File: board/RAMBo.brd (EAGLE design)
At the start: 104.1 x 102.9 mm, 264 parts, among them Q1 PSMN7R0-60YS, Q2 PSMN7R0-60YS, Q3 PSMN7R0-60YS, Q4 IRLML6346TRPBF, Q5 PSMN7R0-60YS, Q8 IRLML6346TRPBF, U1 ATMEGA32U2-MUR, U2 ATMEGA2560-16AU, U3 TPS54332DDA, U4 AD5206, U5 A4982, U6 A4982, U7 A4982, U8 A4982, U9 A4982, X1 C-GRID-02-70543, X10 C-GRID-04-70543, X11 MSTBV10, X12 SPI, X13 EXT-2, X14 C-GRID-04-70543, X15 C-GRID-04-70543, X16 32u2 EXT, X17 3x2M, X18 3x2M, X19 Analog-Ext, X2 USB B-TH, X20 M05PTH, X21 C-GRID-03-70543, X22 C-GRID-03-70543, X23 C-GRID-03-70543, X24 C-GRID-03-70543, X25 C-GRID-03-70543, X26 C-GRID-03-70543, X27 C-GRID-02-70543, X28 C-GRID-02-70543, X29 C-GRID-02-70543, X3 C-GRID-02-70543, X30 C-GRID-02-70543, X31 M05PTH, X32 M05PTH, X33 MSTBA6, X34 PWM_EXT, X39 M05X2PTH, X4 C-GRID-04-70543, X5 C-GRID-02-70543, X6 C-GRID-04-70543, X7 C-GRID-04-70543, X8 C-GRID-04-70543, X9 C-GRID-02-70543, Y1 16MHz KX-7, Y2 16MHz KX-7

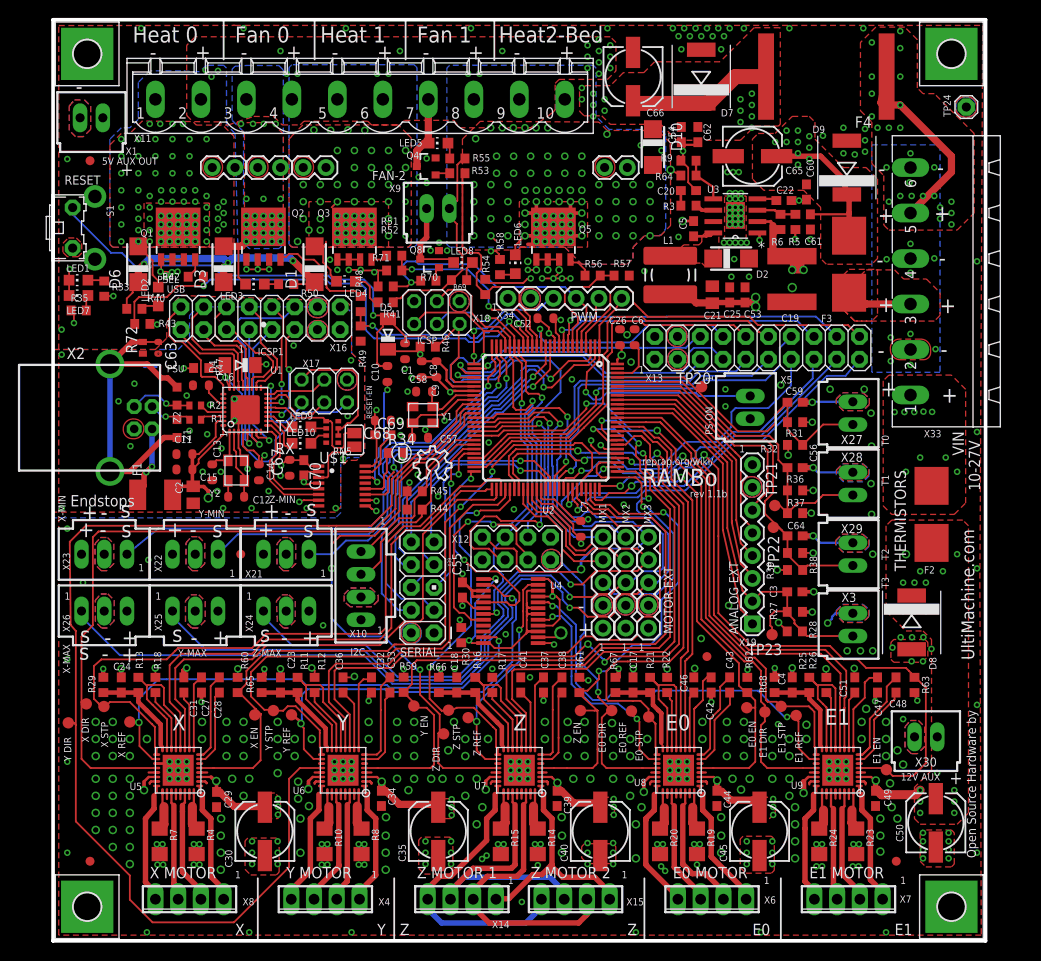
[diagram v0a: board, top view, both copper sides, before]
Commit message: rotate motor and serial ext for easier wave solder
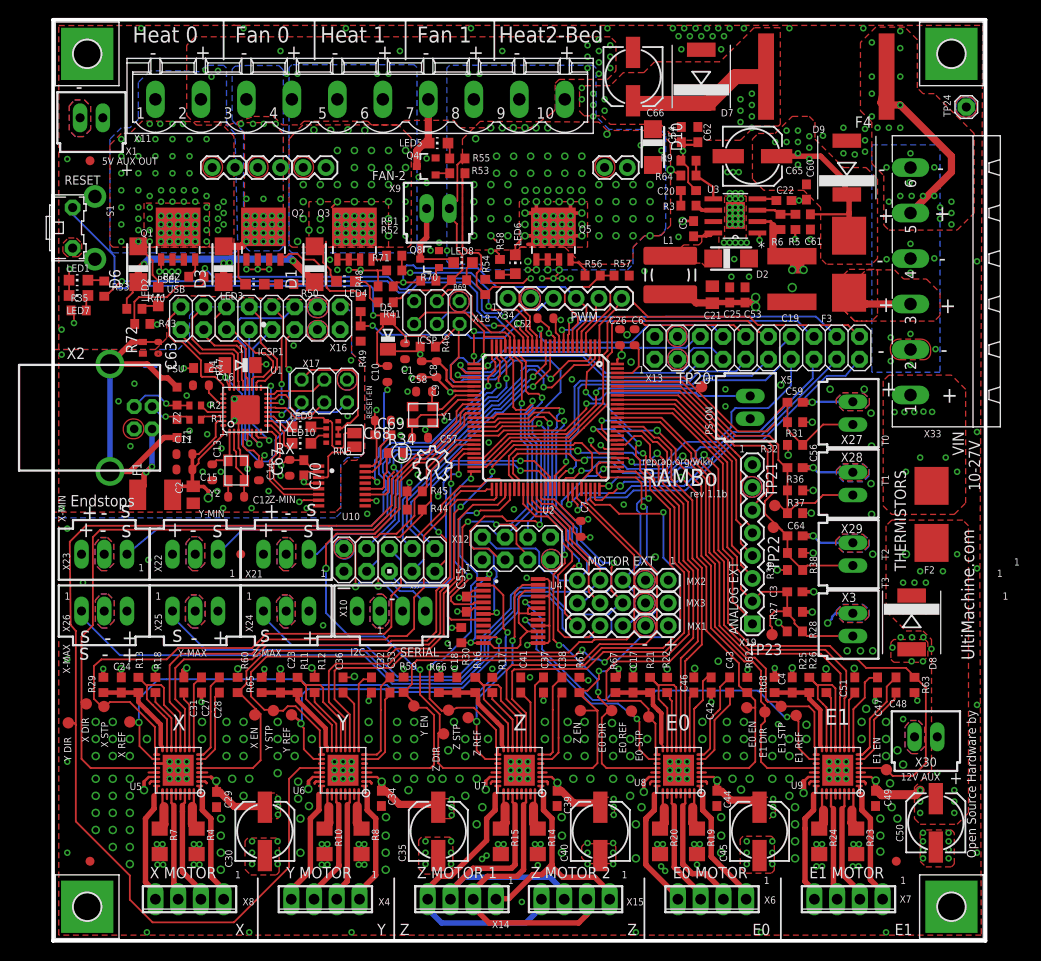
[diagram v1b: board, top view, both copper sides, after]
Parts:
- removed FID5: FIDUCIAL1X2, SparkFun:FIDUCIAL-1X2
- moved X20 7.29 mm to (68.7, 35.2), turned to 180 degrees
- moved X32 5.79 mm to (68.7, 40.3), turned to 180 degrees
- moved X31 5.52 mm to (68.7, 37.7), turned to 180 degrees
- moved X39 4.82 mm to (37.6, 42.5), turned to 90 degrees
- moved X10 4.41 mm to (37.8, 36.8), turned to 0 degrees
- moved C55 1.65 mm to (46.2, 37.6)
- moved R42 0.06 mm to (16.0, 74.2)
- renumbered U$1 to U10
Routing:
- net L13: track 15.4 -> 64.6 mm
- net PC7: track 78.9 -> 61.7 mm, vias 1 -> 0
- net SCL: track 20.1 -> 35.3 mm, vias 0 -> 1
- net PL3: track 57.4 -> 45.3 mm, vias 2 -> 1
- net PC5: track 14.5 -> 25.0 mm
- net PA1: track 94.5 -> 84.3 mm
- net PL5: track 26.4 -> 34.9 mm, vias 1 -> 2
- net TX0: track 55.4 -> 47.0 mm
- net Y-MS2: track 71.1 -> 63.9 mm
- net RX0: track 52.3 -> 45.3 mm
- net PL4: track 30.4 -> 37.2 mm
- net RX1: track 18.1 -> 24.4 mm
- net PB2_MOSI: track 51.8 -> 58.0 mm
- net TX1: track 20.3 -> 25.8 mm
- net Y-EN: track 74.4 -> 69.7 mm
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
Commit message: final connector move, change mount hole for wave
fix drc and silk errors, misc fixes
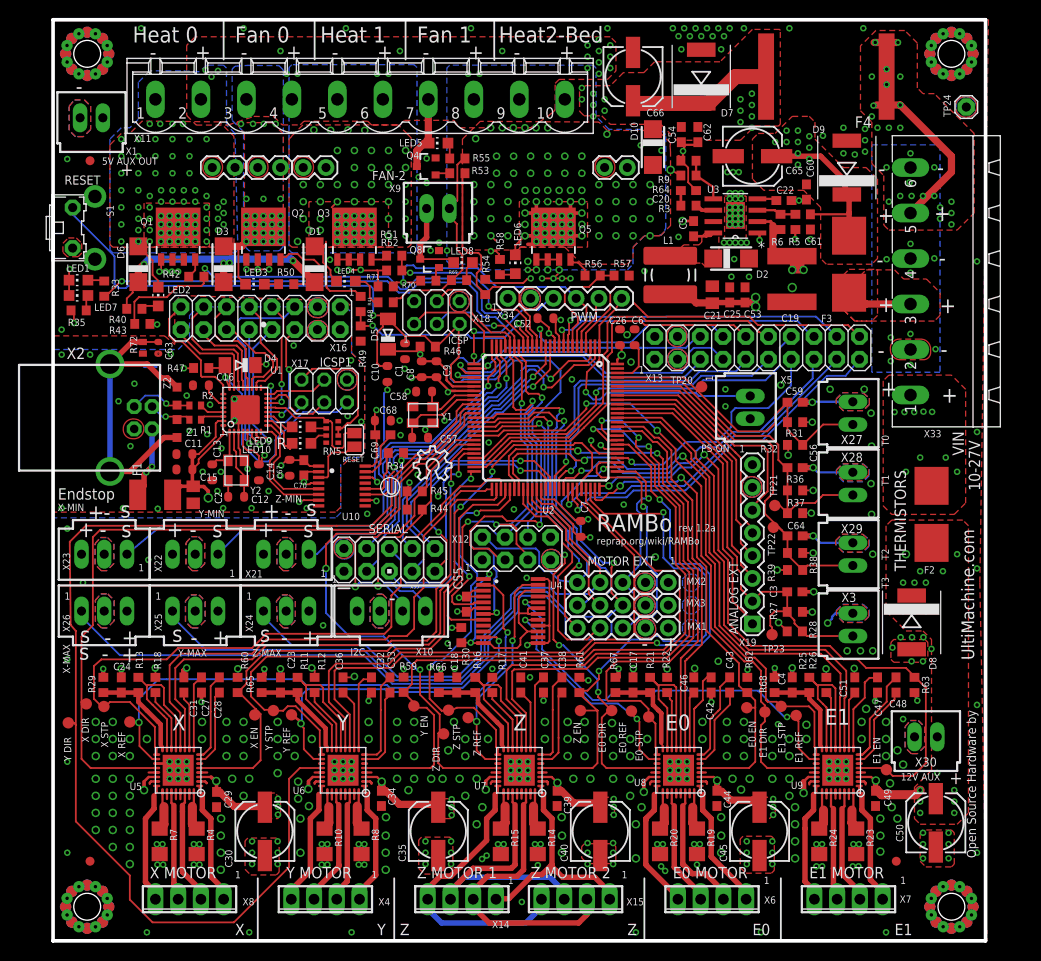
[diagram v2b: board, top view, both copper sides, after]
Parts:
- removed FID4: FIDUCIAL1X2, SparkFun:FIDUCIAL-1X2
- removed H5: MOUNT-PAD-SQUARE3.0, holes:3,0-PAD-SQUARE
- added H4: WAVE-HOLE, ultimachine:3,0-WAVE-HOLE
- H1, H2, H3: value MOUNT-PAD-SQUARE3.0 -> WAVE-HOLE; device holes:3,0-PAD-SQUARE -> ultimachine:3,0-WAVE-HOLE
- moved X32 0.25 mm to (68.7, 40.0)
- moved X20 0.25 mm to (68.7, 34.9)
- moved X31 0.25 mm to (68.7, 37.5)
- renumbered FID6 to FID3
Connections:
- net GND: now also H1.P$1, H1.P$10, H1.P$11, H1.P$12, H1.P$13, H1.P$14, H1.P$15, H1.P$16, H1.P$17, H1.P$18, H1.P$19, H1.P$2, H1.P$20, H1.P$21, H1.P$22, H1.P$23, H1.P$24, H1.P$3, H1.P$4, H1.P$5, H1.P$6, H1.P$7, H1.P$8, H1.P$9, H2.P$1, H2.P$10, H2.P$11, H2.P$12, H2.P$13, H2.P$14, H2.P$15, H2.P$16, H2.P$17, H2.P$18, H2.P$19, H2.P$2, H2.P$20, H2.P$21, H2.P$22, H2.P$23, H2.P$24, H2.P$3, H2.P$4, H2.P$5, H2.P$6, H2.P$7, H2.P$8, H2.P$9, H3.P$1, H3.P$10, H3.P$11, H3.P$12, H3.P$13, H3.P$14, H3.P$15, H3.P$16, H3.P$17, H3.P$18, H3.P$19, H3.P$2, H3.P$20, H3.P$21, H3.P$22, H3.P$23, H3.P$24, H3.P$3, H3.P$4, H3.P$5, H3.P$6, H3.P$7, H3.P$8, H3.P$9, H4.P$1, H4.P$10, H4.P$11, H4.P$12, H4.P$13, H4.P$14, H4.P$15, H4.P$16, H4.P$17, H4.P$18, H4.P$19, H4.P$2, H4.P$20, H4.P$21, H4.P$22, H4.P$23, H4.P$24, H4.P$3, H4.P$4, H4.P$5, H4.P$6, H4.P$7, H4.P$8, H4.P$9; no longer H1.B3,0, H2.B3,0, H3.B3,0, H5.B3,0
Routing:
- net Z-EN: track 56.0 -> 62.4 mm
- net Y-EN: track 69.7 -> 74.6 mm
- net N$16: track 21.6 -> 24.7 mm, vias 21 -> 22
- net Y-MS1: track 79.2 -> 81.1 mm
- net Z-MS1: track 62.1 -> 63.9 mm
- net Z-MS2: track 62.0 -> 63.3 mm
- net GND: track 140.6 -> 141.5 mm, vias 458 -> 456
- net E0-STEP: track 68.9 -> 68.3 mm
- net GND1: vias 25 -> 30
- added copper zone on layer 15, net GND
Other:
- board text added: "Endstop"
- board text added: "R"
- board text added: "T"
- board text added: "reprap.org/wiki/RAMBo"
- board text added: "rev 1.2a"
- board text removed: "Endstops"
- board text removed: "PSEL"
- board text removed: "PSU"
- board text removed: "RESET-EN"
- board text removed: "RX"
- board text removed: "TX"
- board text removed: "USB"
- board text removed: "reprap.org/wiki/"
- board text removed: "rev 1.1b"

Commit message: fix gnd fence
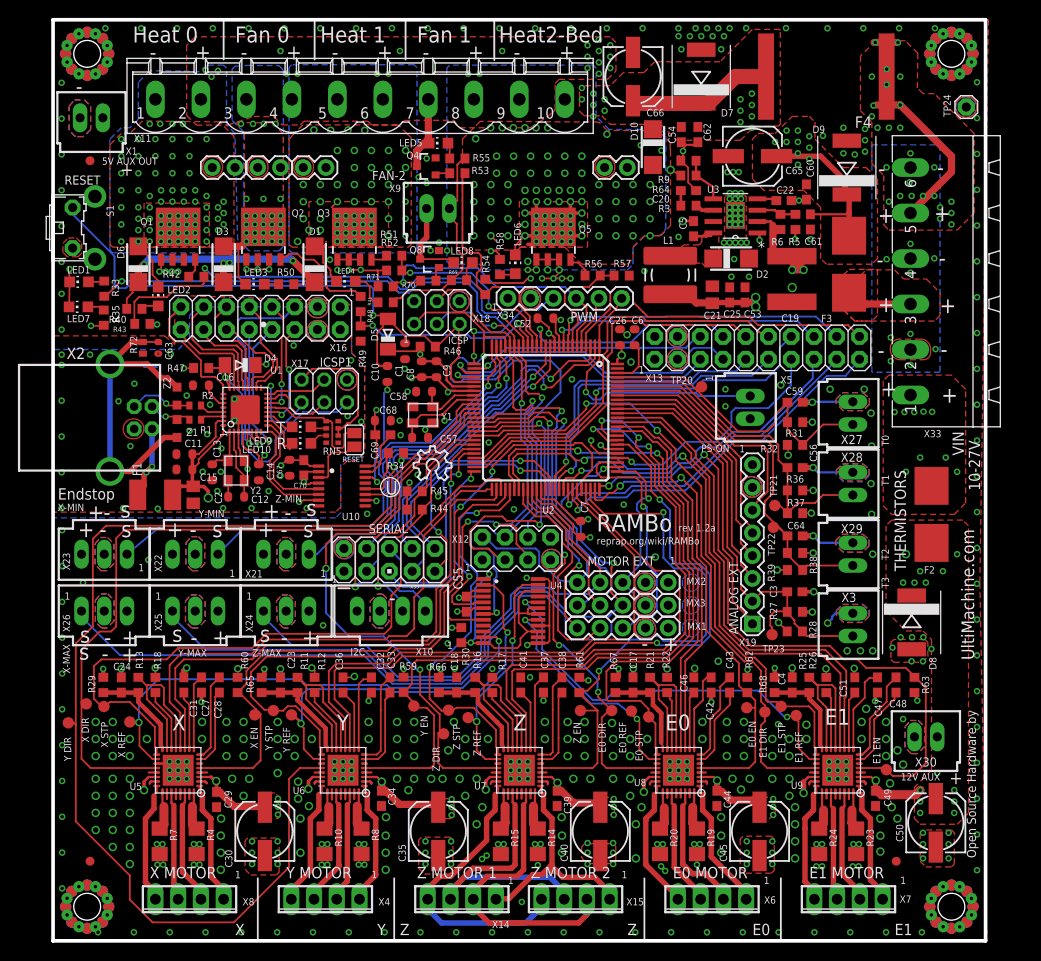
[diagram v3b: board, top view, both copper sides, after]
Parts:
- moved R35 2.92 mm to (5.67, 69.6), turned to 90 degrees
- moved LED7 1.27 mm to (2.84, 70.8)
- moved LED1 0.20 mm to (2.90, 73.6)
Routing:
- net Y-DIR: track 132.9 -> 131.1 mm
- net GND: track 141.5 -> 142.8 mm, vias 456 -> 518
- net X-DIR: track 85.7 -> 84.9 mm
- net GND1: vias 30 -> 34
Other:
- board text added: "Other Layers GTP ---Top Solder Paste OLN -- Board outline TXT -- Drill 2.4 leading suppression"
- board text added: "Panelize with second PCB here."
- board text added: "Stack Up GTO ------ Top Silk GTS - Solder Mask GTL------------ 1oz 0.61mm G2L ----------- 2oz 0.2mm G3L ----------- 2oz 0.61mm GBL ----------- 1oz GBS - Solder Mask Total Thickness ~ 1.62mm"

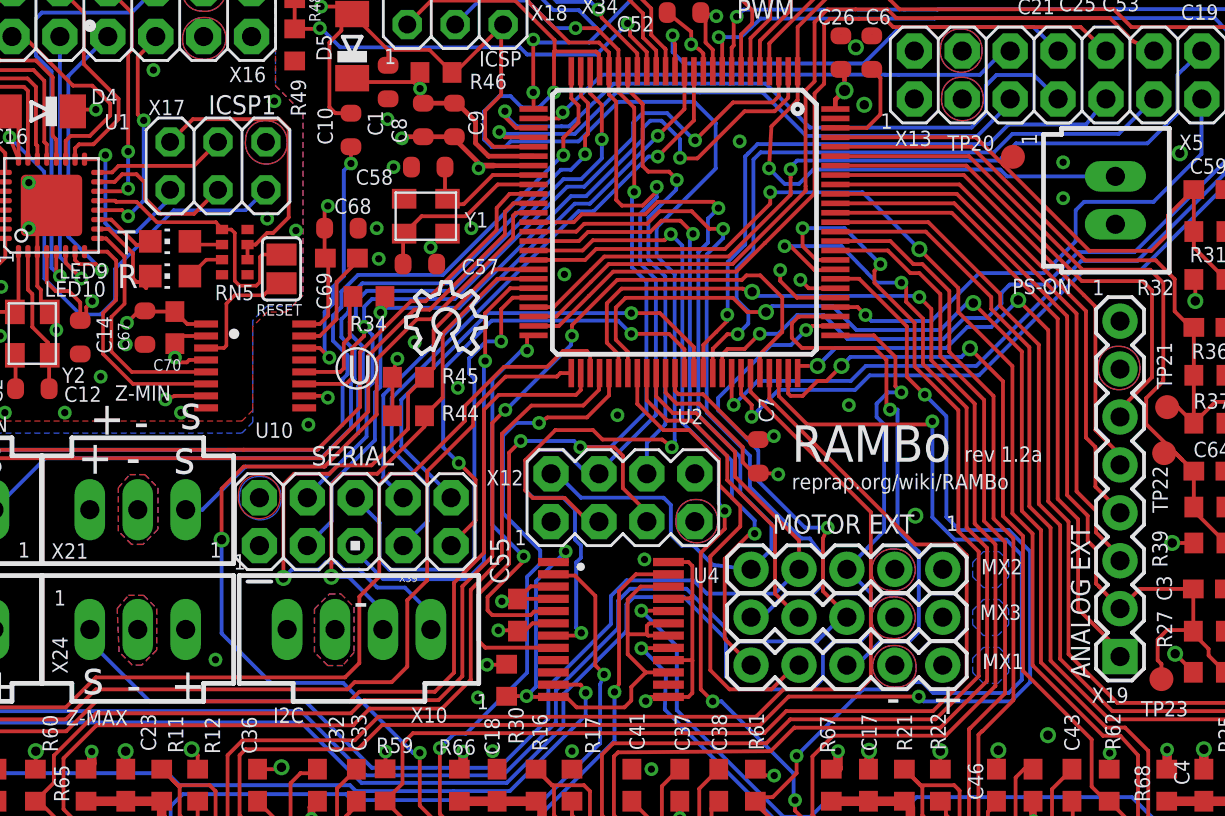
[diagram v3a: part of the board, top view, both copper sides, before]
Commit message: change thieve style, rst-en trace added back,
DTR resistor now pull up - now back to original usb reset behaviour of
Rambo
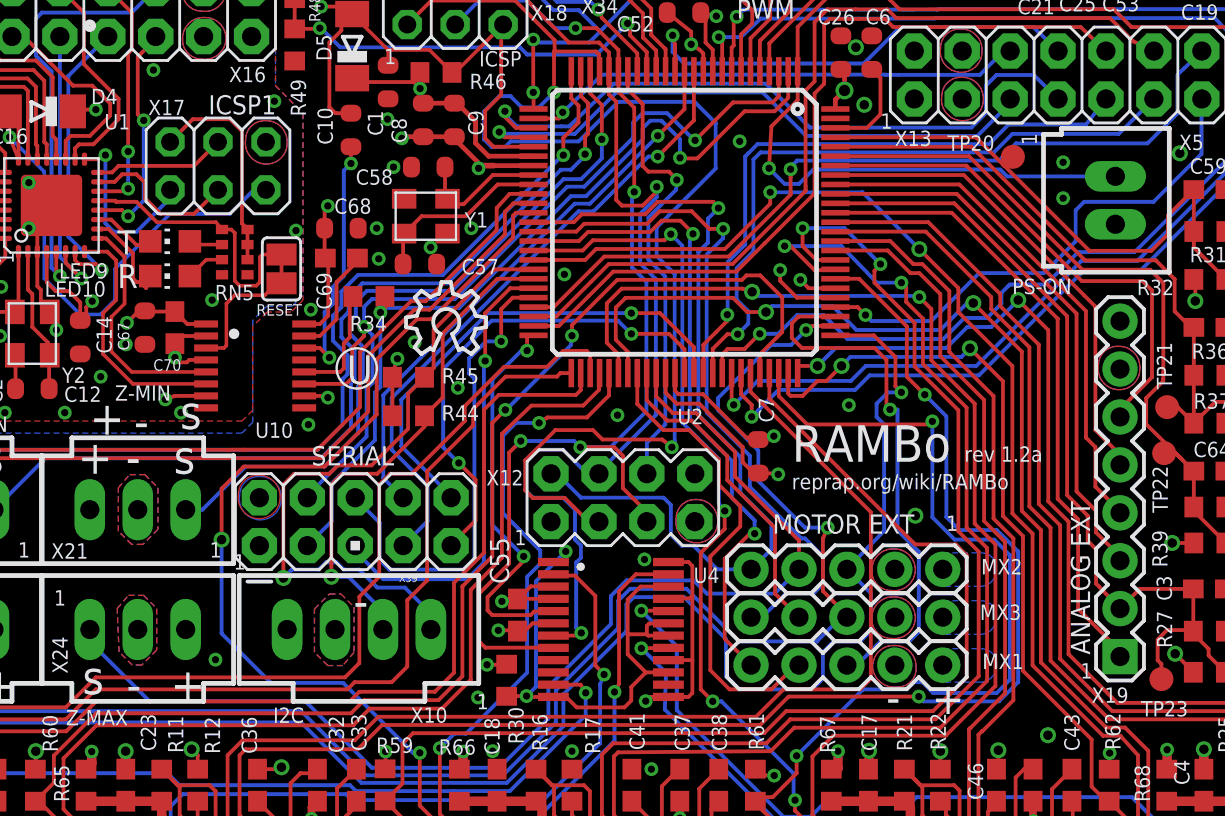
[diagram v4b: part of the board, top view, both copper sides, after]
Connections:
- removed net RESET-I: JP2.2, U10.3
- net DTR: now also JP2.2, U10.3
- net GND1: no longer RN5.4
- net USBVCC: now also RN5.4
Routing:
- net DTR: track 14.6 -> 22.8 mm
- net RESET-I: track 6.72 -> 0.00 mm
- net USBVCC: track 52.2 -> 48.4 mm
- net Y-MS1: track 81.1 -> 79.8 mm
- net Z-EN: track 62.4 -> 61.1 mm
- net GND: vias 518 -> 519
- added copper zone on layer 16, net VCC
